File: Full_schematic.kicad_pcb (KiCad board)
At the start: 8 copper layers, 349 parts, among them IC1 XC7A100T-1FTG256C, J1 FFC3B11-40-T, J3 Conn_ST_STDC14, J5 USB_B_Micro, J6 AHDF15A-KG-TAXB, U1 2S7A_0518S1U, U10 MC14511BDG, U11 MAN72A, U12 MC14511BDG, U13 STM32U545VETxQ, U14 MAN72A, U15 MC14511BDG, U16 MAN72A, U17 MC14511BDG, U18 PTS645SM43SMTR92LFS, U19 PTS645SM43SMTR92LFS, U2 IS66WVE4M16EBLL-70BLI, U3 TPS54294PWP, U4 TPS54325PWPR, U5 SN74ALVC245PWR, U6 IS66WVE4M16EBLL-70BLI, U7 S25FL127S, U8 SN74ALVC245PWR, U9 MAN72A, Y1 ASCO, Y2 48MHz

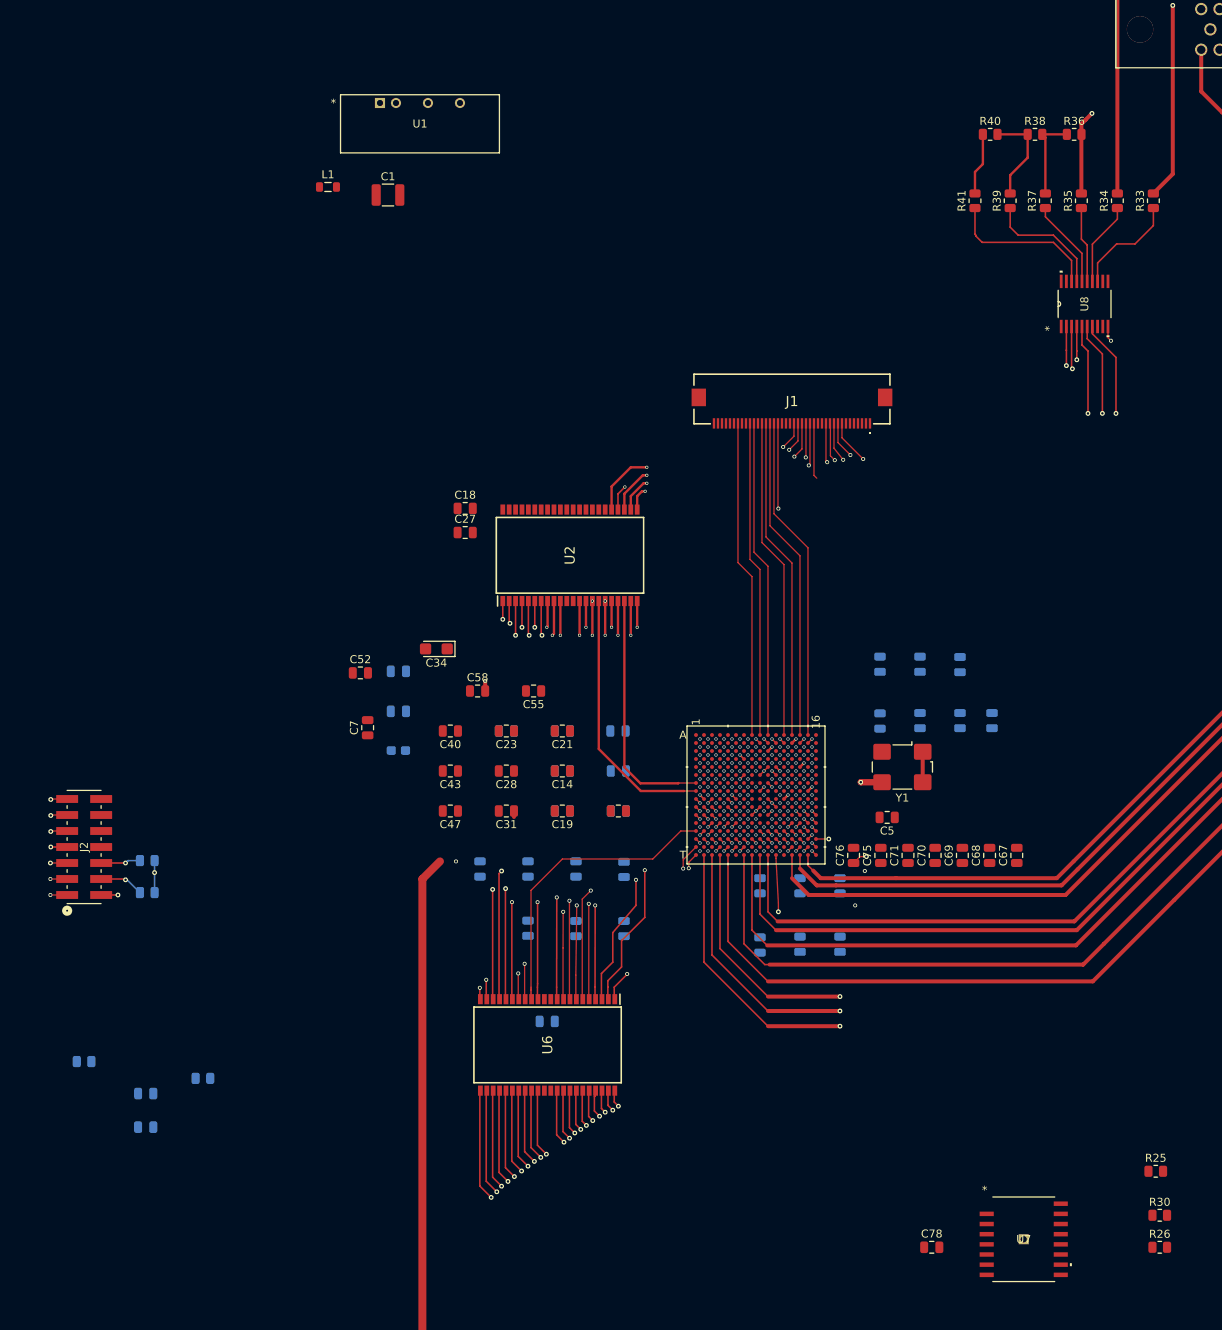
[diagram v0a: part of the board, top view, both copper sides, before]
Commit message: Connected debug conn to fpga ++
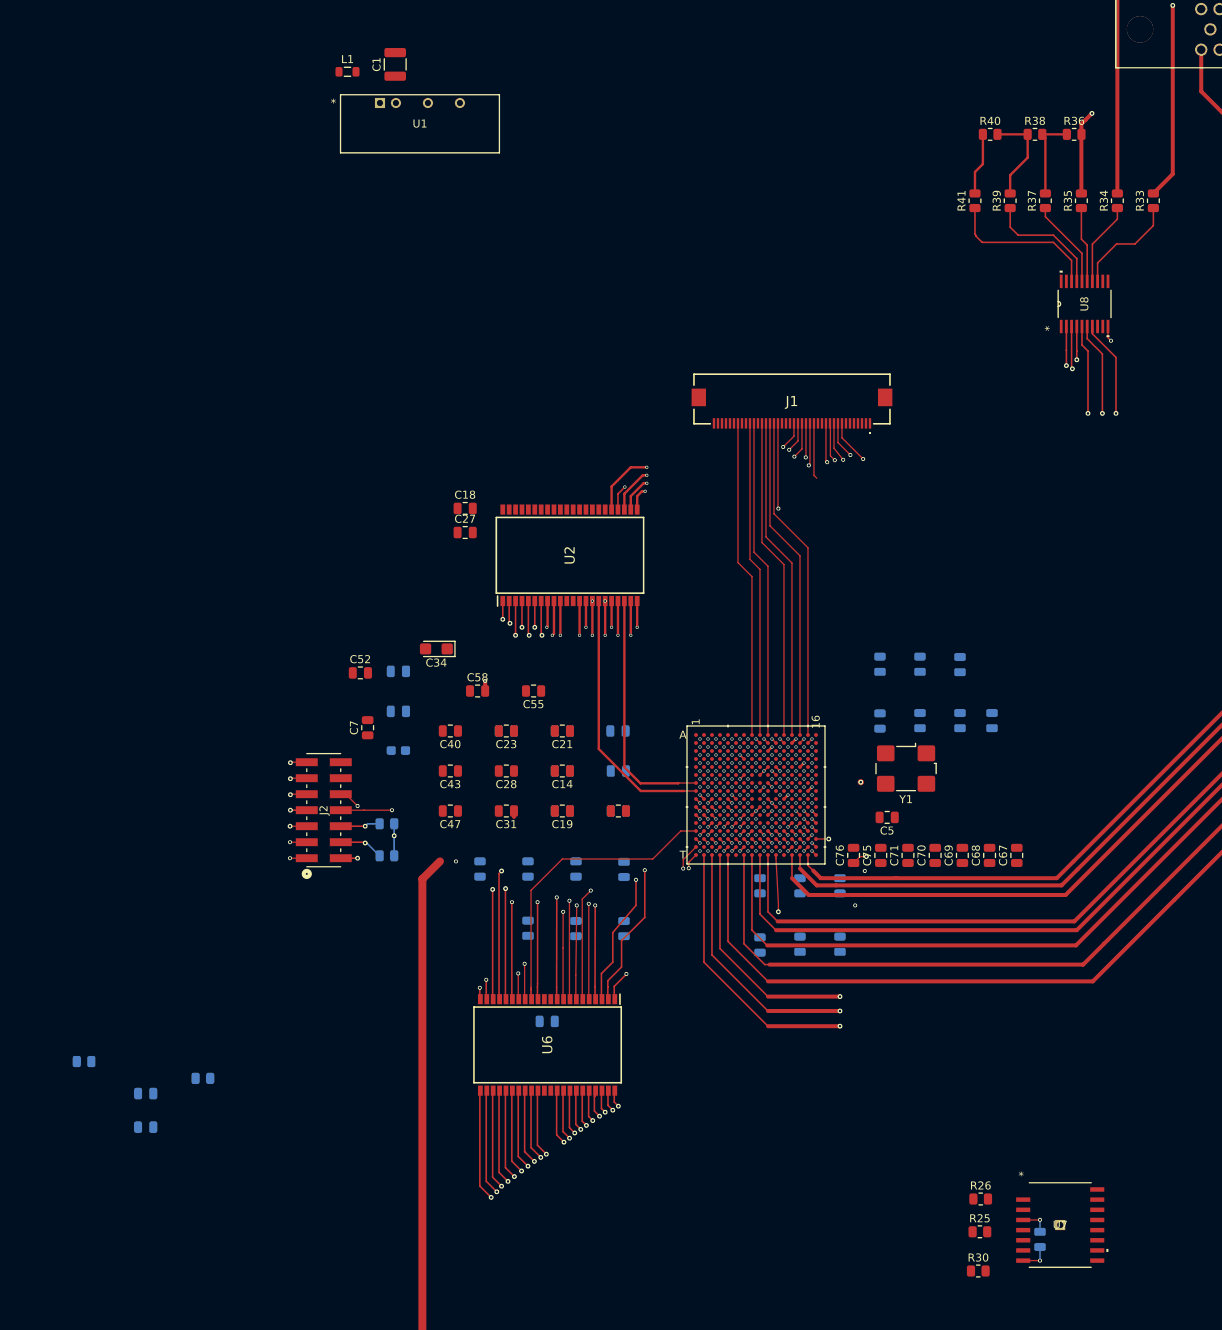
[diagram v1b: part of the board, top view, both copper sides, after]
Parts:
- C78: moved to B.Cu
- moved J2 30.3 mm to (63.8, 132.7)
- moved R23 30.3 mm to (71.7, 138.4)
- moved R28 30.3 mm to (71.7, 134.4)
- moved R30 23.7 mm to (145.6, 190.3)
- moved R25 23.2 mm to (145.8, 185.4)
- moved R26 23.2 mm to (145.9, 181.3)
- moved C1 16.3 mm to (72.7, 39.5), turned to 90 degrees
- moved L1 14.6 mm to (66.7, 40.4)
- moved C78 13.6 mm to (153.3, 186.3), turned to 90 degrees
- moved U7 4.90 mm to (155.8, 184.6)
- moved Y1 0.50 mm to (136.6, 127.5)
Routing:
- net Net-(IC1-TDI_0): track 0.00 -> 53.1 mm, vias 0 -> 2
- net Net-(IC1-TDO_0): track 0.00 -> 52.9 mm, vias 0 -> 2
- net Net-(IC1-TMS_0): track 5.55 -> 56.6 mm, vias 1 -> 2
- net Net-(IC1-TCK_0): track 4.97 -> 55.6 mm, vias 1 -> 2
- net P4: track 29.8 -> 25.9 mm
- net +3V3: track 45.8 -> 42.0 mm
- net Net-(U7-VCC): track 0.00 -> 3.80 mm, vias 0 -> 1
- net Net-(U7-VSS): track 0.00 -> 3.61 mm, vias 0 -> 1
- net Net-(IC1-IO_L14P_T2_SRCC_15): track 13.8 -> 11.1 mm
- net N3: track 36.5 -> 35.5 mm
- net N2: track 37.4 -> 36.6 mm
- net (no net): vias 100 -> 96

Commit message: finished first draft of pcb
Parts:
- removed the C1 at (-181.2, 131.6)
- removed the C10 at (-225.5, 128.6)
- removed the C11 at (-225.5, 131.6)
- removed the C12 at (-225.5, 134.6)
- removed the C13 at (-221.1, 104.5)
- removed the C14 at (-221.1, 107.5)
- removed the C15 at (-221.1, 110.5)
- removed the C16 at (-221.1, 113.5)
- removed the C17 at (-221.1, 116.6)
- removed C18, C27: 100n, Capacitor_SMD:C_0805_2012Metric
- removed the C19 at (-221.1, 119.6)
- removed the C2 at (-225.5, 104.5)
- removed the C20 at (-221.1, 122.6)
- removed the C21 at (-221.1, 125.6)
- removed the C22 at (-221.1, 128.6)
- removed the C23 at (-221.1, 131.6)
- removed the C24 at (-221.1, 134.6)
- removed the C25 at (-216.6, 104.5)
- removed the C26 at (-216.6, 107.5)
- removed the C28 at (-216.6, 110.5)
- removed the C29 at (-216.6, 113.5)
- removed the C3 at (-225.5, 107.5)
- removed the C30 at (-216.6, 116.6)
- removed the C31 at (-216.6, 119.6)
- removed the C32 at (-216.6, 122.6)
- removed the C33 at (-216.6, 125.6)
- removed the C34 at (-172.5, 137.7)
- removed the C35 at (-172.4, 125.3)
- removed the C36 at (-216.6, 128.6)
- removed the C37 at (-216.6, 131.6)
- removed the C38 at (-216.6, 134.6)
- removed the C39 at (-212.2, 104.5)
- removed the C4 at (-225.5, 110.5)
- removed the C40 at (-212.2, 107.5)
- removed the C41 at (-212.2, 110.5)
- removed the C42 at (-212.2, 113.5)
- removed the C43 at (-212.2, 116.6)
- removed the C44 at (-212.2, 119.6)
- removed the C45 at (-212.2, 122.6)
- removed the C46 at (-212.2, 125.6)
- removed the C47 at (-212.2, 128.6)
- removed the C48 at (-212.2, 131.6)
- removed the C49 at (-212.2, 134.6)
- removed the C5 at (-225.5, 113.5)
- removed the C50 at (-207.7, 104.5)
- removed the C51 at (-207.7, 107.5)
- removed the C52 at (-207.7, 110.5)
- removed the C53 at (-207.7, 113.5)
- removed the C54 at (-207.7, 116.6)
- removed the C55 at (-207.7, 119.6)
- removed the C56 at (-207.7, 122.6)
- removed the C57 at (-207.7, 125.6)
- removed the C58 at (-207.7, 128.6)
- removed the C59 at (-207.7, 131.6)
- removed the C6 at (-225.5, 116.6)
- removed the C60 at (-207.7, 134.6)
- removed the C61 at (-203.2, 104.5)
- removed the C62 at (-203.2, 107.5)
- removed the C63 at (-203.2, 110.5)
- removed the C64 at (-203.2, 113.5)
- removed the C65 at (-203.2, 116.6)
- removed the C66 at (-203.2, 119.6)
- removed the C67 at (-203.2, 122.6)
- removed the C68 at (-203.2, 125.6)
- removed the C69 at (-203.2, 128.6)
- removed the C7 at (-225.5, 119.6)
- removed the C70 at (-203.2, 131.6)
- removed the C71 at (-203.2, 134.6)
- removed the C72 at (-198.8, 104.5)
- removed the C73 at (-198.8, 107.5)
- removed the C74 at (-198.8, 110.5)
- removed the C75 at (-198.8, 113.5)
- removed the C76 at (-198.8, 116.6)
- removed the C77 at (-198.8, 119.6)
- removed the C78 at (-198.8, 122.6)
- removed the C8 at (-225.5, 122.6)
- removed the C9 at (-225.5, 125.6)
- removed the D1 at (-172.5, 141.0)
- removed the J1 at (-182.5, 107.7)
- removed the J2 at (-177.9, 149.1)
- removed the J5 at (-189.5, 118.2)
- removed the L1 at (-172.4, 114.3)
- removed the L2 at (-172.4, 117.0)
- removed the L3 at (-172.4, 119.8)
- removed the L4 at (-172.4, 122.5)
- removed the R1 at (-225.5, 137.6)
- removed the R10 at (-221.1, 137.6)
- removed the R12 at (-221.1, 140.6)
- removed the R13 at (-221.1, 143.5)
- removed the R14 at (-221.1, 146.4)
- removed the R15 at (-221.1, 149.4)
- removed the R16 at (-221.1, 152.3)
- removed the R17 at (-221.1, 155.3)
- removed the R18 at (-221.1, 158.2)
- removed the R19 at (-221.1, 161.2)
- removed the R2 at (-225.5, 140.6)
- removed the R20 at (-216.7, 137.6)
- removed the R21 at (-216.7, 140.6)
- removed the R22 at (-216.7, 143.5)
- removed the R23 at (-216.7, 146.4)
- removed the R24 at (-216.7, 149.4)
- removed the R25 at (-216.7, 152.3)
- removed the R26 at (-216.7, 155.3)
- removed the R27 at (-216.7, 158.2)
- removed the R28 at (-216.7, 161.2)
- removed the R29 at (-212.3, 137.6)
- removed the R3 at (-225.5, 143.5)
- removed the R30 at (-212.3, 140.6)
- removed the R31 at (-212.3, 143.5)
- removed the R32 at (-212.3, 146.4)
- removed the R33 at (-212.3, 149.4)
- removed the R34 at (-212.3, 152.3)
- removed the R35 at (-212.3, 155.3)
- removed the R36 at (-212.3, 158.2)
- removed the R37 at (-212.3, 161.2)
- removed the R38 at (-207.9, 137.6)
- removed the R39 at (-207.9, 140.6)
- removed the R4 at (-225.5, 146.4)
- removed the R40 at (-207.9, 143.5)
- removed the R41 at (-207.9, 146.4)
- removed the R5 at (-225.5, 149.4)
- removed the R6 at (-225.5, 152.3)
- removed the R7 at (-225.5, 155.3)
- removed the R8 at (-225.5, 158.2)
- removed the R9 at (-225.5, 161.2)
- removed REF**: NetTie-2_SMD_Pad0.5mm, NetTie:NetTie-2_SMD_Pad0.5mm
- removed the U1 at (-200.0, 137.9)
- removed the U3 at (-192.1, 125.0)
- removed the U4 at (-192.1, 131.8)
- removed the U5 at (-179.3, 117.0)
- removed the U7 at (-180.7, 159.4)
- removed the U8 at (-179.3, 125.3)
- removed the Y1 at (-179.9, 139.8)
- C31, C52, C55, C58, C69, C7, C76, L4, R10, R9: moved to B.Cu
- U7: footprint footprints:SO3016_INF -> fpga_flash:SOIC127P800X216-8N
- Y1: value ASCO -> 100Hz; footprint Oscillator:Oscillator_SMD_SiT_PQFN-4Pin_7.0x5.0mm -> 100Hz_crystal:CB3LV3C100M000000
- moved C53 122.2 mm to (163.7, 165.7), turned to 90 degrees
- moved C77 122.2 mm to (163.7, 170.7), turned to -90 degrees
- moved R6 121.4 mm to (208.2, 166.0), turned to 90 degrees
- moved R13 120.7 mm to (154.5, 161.8)
- moved D1 120.6 mm to (208.2, 172.3), turned to 90 degrees
- moved R5 115.8 mm to (204.2, 166.0), turned to 90 degrees
- moved L1 115.3 mm to (170.8, 90.0), turned to -90 degrees
- moved U1 113.6 mm to (174.3, 91.1), turned to 90 degrees
- moved C52 110.7 mm to (171.3, 156.2), turned to 90 degrees
- moved R12 109.5 mm to (157.8, 157.7)
- moved C1 107.0 mm to (170.1, 83.7), turned to -90 degrees
- moved C7 105.4 mm to (167.2, 161.2), turned to -90 degrees
- moved C39 100.7 mm to (167.2, 156.2), turned to 90 degrees
- moved C44 99.0 mm to (167.2, 146.2), turned to 90 degrees
- moved C40 97.6 mm to (171.3, 156.2), turned to 90 degrees
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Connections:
- C62 pad 1: +3.3V -> +3V3
- C64 pad 1: +3.3V -> +3V3
- C94 pad 1: +3.3V -> +3V3
- J4 pad G1: (no net) -> GND
- J4 pad G2: (no net) -> GND
- L4 pad 2: +3.3V -> +3V3
- R12 pad 2: +3.3V -> +3V3
- R13 pad 2: +3.3V -> +3V3
- R33 pad 2: VSYNC -> VGA_VSYNC
- R42 pad B1A: (no net) -> PE9
- R42 pad B2A: (no net) -> GND
- R42 pad H1: (no net) -> +3V3
- R42 pad H2: (no net) -> PC3
- R42 pad H3: (no net) -> GND
- R42 pad V1: (no net) -> +3V3
- R42 pad V2: (no net) -> PC2
- R42 pad V3: (no net) -> GND
- R45 pad 2: +3.3V -> +3V3
- R9 pad 1: +3.3V -> +3V3
- U10 pad 16: +3.3V -> +3V3
- U10 pad 3: +3.3V -> +3V3
- U10 pad 4: +3.3V -> +3V3
- U12 pad 16: +3.3V -> +3V3
- U12 pad 3: +3.3V -> +3V3
- U12 pad 4: +3.3V -> +3V3
- U15 pad 16: +3.3V -> +3V3
- U15 pad 3: +3.3V -> +3V3
- U15 pad 4: +3.3V -> +3V3
- U17 pad 16: +3.3V -> +3V3
- U17 pad 3: +3.3V -> +3V3
- U17 pad 4: +3.3V -> +3V3
- U5 pad 1: +3.3V -> +3V3
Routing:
- net GND: track 192.5 -> 328.9 mm, vias 65 -> 120
- net +3V3: track 42.0 -> 168.2 mm, vias 31 -> 60
- net PD11: track 184.4 -> 102.1 mm
- net FPGA_DONE: track 0.00 -> 74.4 mm, vias 0 -> 2
- net Net-(IC1-IO_L1P_T0_AD4P_35): track 0.00 -> 72.6 mm, vias 0 -> 2
- net Net-(IC1-IO_L2P_T0_AD12P_35): track 0.00 -> 70.5 mm, vias 0 -> 2
- net MCU_CS: track 0.00 -> 69.9 mm, vias 0 -> 2
- net Net-(IC1-IO_L10N_T1_AD11N_15): track 6.99 -> 76.1 mm
- net B5: track 0.00 -> 68.4 mm, vias 1 -> 2
- net B4: track 0.00 -> 67.9 mm, vias 1 -> 2
- net MCU_SCK: track 0.00 -> 66.8 mm, vias 0 -> 2
- net A2: track 0.00 -> 66.0 mm, vias 0 -> 2
- net C2: track 0.00 -> 59.9 mm, vias 1 -> 2
- net MCU_MOSI: track 0.00 -> 59.6 mm, vias 0 -> 2
- net C1: track 0.00 -> 58.0 mm, vias 1 -> 2
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- added copper zone on In3.Cu, net +1V8
- added copper zone on In3.Cu, net Net-(J5-VBUS)
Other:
- board outline added: 215 x 184.5 mm

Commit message: commit melding
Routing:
- net Net-(U3-EN2): track 10.7 -> 18.3 mm, vias 0 -> 2
- net +3V3: track 168.2 -> 171.6 mm
- net GND: track 328.9 -> 329.3 mm, vias 120 -> 119
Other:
- board size 215 x 184.5 mm -> 215 x 178.7 mm
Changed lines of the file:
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@@
 	)
 	(gr_rect
-		(start 114.7 40.476105)
+		(start 114.7 46.276105)
 		(end 329.7 224.976105)
 		(stroke
@@
 	)
 	(segment
+		(start 152.898001 156.676106)
+		(end 152.422001 157.152106)
+		(width 0.15)
+		(layer "In3.Cu")
+		(net 2)
+	)
+	(segment
+		(start 150.422001 157.152106)
+		(end 149.898001 157.676106)
+		(width 0.15)
+		(layer "In3.Cu")
+		(net 2)
+	)
+	(segment
+		(start 152.422001 157.152106)
+		(end 150.422001 157.152106)
+		(width 0.15)
+		(layer "In3.Cu")
+		(net 2)
+	)
+	(segment
 		(start 171.3 157.126105)
 		(end 169.271475 159.15463)
@@
 	)
 	(segment
+		(start 163.3 206.9)
+		(end 163.2 206.8)
+		(width 0.2)
+		(layer "F.Cu")
+		(net 64)
+	)
+	(segment
 		(start 157.400001 151.176105)
 		(end 157.400001 151.178106)
@@
 	)
 	(segment
+		(start 163.3 206.9)
+		(end 163.670966 207.270966)
+		(width 0.2)
+		(layer "F.Cu")
+		(net 64)
+	)
+	(segment
 		(start 218.725 146.406105)
 		(end 218.725 147.231105)
@@
 	)
 	(segment
-		(start 163.670966 207.749299)
-		(end 164.022999 207.397266)
-		(width 0.15)
-		(layer "F.Cu")
-		(net 64)
-	)
-	(segment
 		(start 152.4 148.176105)
 		(end 152.4 148.174107)
@@
 	)
 	(segment
-		(start 164.922999 203.997266)
-		(end 164.922999 202.924257)
-		(width 0.2)
-		(layer "F.Cu")
-		(net 64)
-	)
-	(segment
 		(start 224.598002 89.476106)
 		(end 224.598002 87.580103)
@@
 	)
 	(segment
-		(start 163.670966 208.718267)
-		(end 163.670966 207.749299)
-		(width 0.15)
-		(layer "F.Cu")
-		(net 64)
-	)
-	(segment
 		(start 186.224997 221.620269)
 		(end 186.222998 221.622268)
@@
 	)
 	(segment
+		(start 163.2 206.8)
+		(end 162.2 206.8)
+		(width 0.2)
+		(layer "F.Cu")
+		(net 64)
+	)
+	(segment
 		(start 273.1 91.376105)
 		(end 273.1 92.650701)
@@
 	)
 	(segment
+		(start 164.320977 208.718267)
+		(end 164.320977 207.920977)
+		(width 0.2)
+		(layer "F.Cu")
+		(net 64)
+	)
+	(segment
 		(start 162.398001 158.176106)
 		(end 161.898001 157.676106)
@@
 	)
 	(segment
-		(start 164.322999 208.716245)
-		(end 164.320977 208.718267)
-		(width 0.3)
-		(layer "F.Cu")
-		(net 64)
-	)
-	(segment
 		(start 202.925 148.531105)
 		(end 201.325 150.131105)
@@
 	)
 	(segment
+		(start 164.320977 207.920977)
+		(end 163.3 206.9)
+		(width 0.2)
+		(layer "F.Cu")
+		(net 64)
+	)
+	(segment
 		(start 156.400001 150.176105)
 		(end 156.385994 150.176105)
@@
 	)
 	(segment
-		(start 165.621 204.695267)
-		(end 164.922999 203.997266)
-		(width 0.15)
-		(layer "F.Cu")
-		(net 64)
-	)
-	(segment
 		(start 317.2 119.256105)
 		(end 317.2 120.881105)
@@
 	)
 	(segment
-		(start 164.022999 207.397266)
-		(end 164.322999 207.697266)
-		(width 0.3)
-		(layer "F.Cu")
-		(net 64)
-	)
-	(segment
 		(start 171.823 218.003165)
 		(end 171.823 220.022268)
@@
 	)
 	(segment
+		(start 164.322999 208.716245)
+		(end 164.320977 208.718267)
+		(width 0.3)
+		(layer "F.Cu")
+		(net 64)
+	)
+	(segment
 		(start 152.898001 158.674107)
 		(end 152.4 158.176106)
@@
 	)
 	(segment
-		(start 164.322999 207.697266)
-		(end 164.322999 208.716245)
-		(width 0.3)
+		(start 163.670966 207.270966)
+		(end 163.670966 208.718267)
+		(width 0.2)
 		(layer "F.Cu")
 		(net 64)
@@
 	)
 	(via
-		(at 164.022999 207.397266)
+		(at 162.2 206.8)
 		(size 0.6)
 		(drill 0.3)
@@
 		(net 64)
 	)
-	(via
-		(at 164.922999 203.997266)
-		(size 0.6)
-		(drill 0.3)
-		(layers "F.Cu" "B.Cu")
-		(net 64)
-	)
 	(segment
 		(start 151.7 164.776105)
@@
 		(end 164.022999 204.197267)
 		(width 0.2)
-		(layer "In2.Cu")
+		(layer "In5.Cu")
 		(net 75)
 	)
@@
 		(end 167.951841 208.126109)
 		(width 0.2)
-		(layer "In2.Cu")
+		(layer "In5.Cu")
 		(net 75)
 	)
@@
 	)
 	(segment
-		(start 186.393199 208.076108)
-		(end 187.042 208.076108)
+		(start 181.2 208.726106)
+		(end 178.726106 208.726106)
 		(width 0.15)
 		(layer "F.Cu")
@@
 	)
 	(segment
-		(start 185.5 209.376105)
-		(end 186 208.876105)
+		(start 188.2 208.1)
+		(end 188.2 208.076108)
 		(width 0.15)
 		(layer "F.Cu")
@@
 	)
 	(segment
-		(start 186 208.469307)
-		(end 186.393199 208.076108)
-		(width 0.15)
+		(start 190.275302 208.076108)
+		(end 190.319103 208.032307)
+		(width 0.2)
 		(layer "F.Cu")
 		(net 284)
 	)
 	(segment
-		(start 182.808998 209.376105)
-		(end 185.5 209.376105)
+		(start 186.393199 208.076108)
+		(end 187.042 208.076108)
 		(width 0.15)
 		(layer "F.Cu")
@@
 	)
 	(segment
-		(start 190.275302 208.076108)
-		(end 190.319103 208.032307)
+		(start 187.042 208.076108)
+		(end 188.2 208.076108)
 		(width 0.2)
 		(layer "F.Cu")
@@
 	)
 	(segment
-		(start 182.158999 208.726106)
-		(end 182.808998 209.376105)
+		(start 188.7 208.6)
+		(end 188.2 208.1)
 		(width 0.15)
 		(layer "F.Cu")
@@
 	)
 	(segment
-		(start 187.042 208.076108)
+		(start 188.2 208.076108)
 		(end 190.275302 208.076108)
 		(width 0.2)
@@
 		(net 284)
 	)
+	(via
+		(at 178.7 208.7)
+		(size 0.6)
+		(drill 0.3)
+		(layers "F.Cu" "B.Cu")
+		(net 284)
+	)
+	(via
+		(at 188.7 208.6)
+		(size 0.5)
+		(drill 0.3)
+		(layers "F.Cu" "B.Cu")
+		(net 284)
+	)
 	(segment
-		(start 186 208.876105)
-		(end 186 208.469307)
+		(start 186.9 208.7)
+		(end 188.6 208.7)
 		(width 0.15)
-		(layer "F.Cu")
+		(layer "In2.Cu")
 		(net 284)
 	)
 	(segment
-		(start 181.249999 208.776105)
-		(end 181.2 208.726106)
-		(width 0.2)
-		(layer "F.Cu")
+		(start 184.8 209.6)
+		(end 185.1 209.6)
+		(width 0.15)
+		(layer "In2.Cu")
 		(net 284)
 	)
 	(segment
-		(start 181.2 208.726106)
-		(end 182.158999 208.726106)
+		(start 186 209.6)
+		(end 186.9 208.7)
 		(width 0.15)
-		(layer "F.Cu")
+		(layer "In2.Cu")
+		(net 284)
+	)
+	(segment
+		(start 188.6 208.7)
+		(end 188.7 208.6)
+		(width 0.15)
+		(layer "In2.Cu")
+		(net 284)
+	)
+	(segment
+		(start 185.1 209.6)
+		(end 186 209.6)
+		(width 0.15)
+		(layer "In2.Cu")
+		(net 284)
+	)
+	(segment
+		(start 179.6 209.6)
+		(end 184.8 209.6)
+		(width 0.15)
+		(layer "In2.Cu")
+		(net 284)
+	)
+	(segment
+		(start 178.7 208.7)
+		(end 179.6 209.6)
+		(width 0.15)
+		(layer "In2.Cu")
 		(net 284)
 	)
